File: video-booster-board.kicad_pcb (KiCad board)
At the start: 4 copper layers, 36.5 x 41.5 mm, 122 parts, among them J1 0473460001, J10 MC-HVT1-S04-G, J2 HDMI-PE10-19-LF, J3 HDMI-PE10-19-LF, J4 M20-9990246, J5 M20-9990246, J6 685119134923_, J7 M20-9990246, J8 M20-9990246, J9 685119134923_, Q1 BC817W, Q2 BC817W, U1 PTN3363, U2 EFM32HG309, U3 PTN3363, U4 LP2985-33DBVR, U5 PCA9554BS3, U6 PCA9517ADP, U7 PCA9517ADP

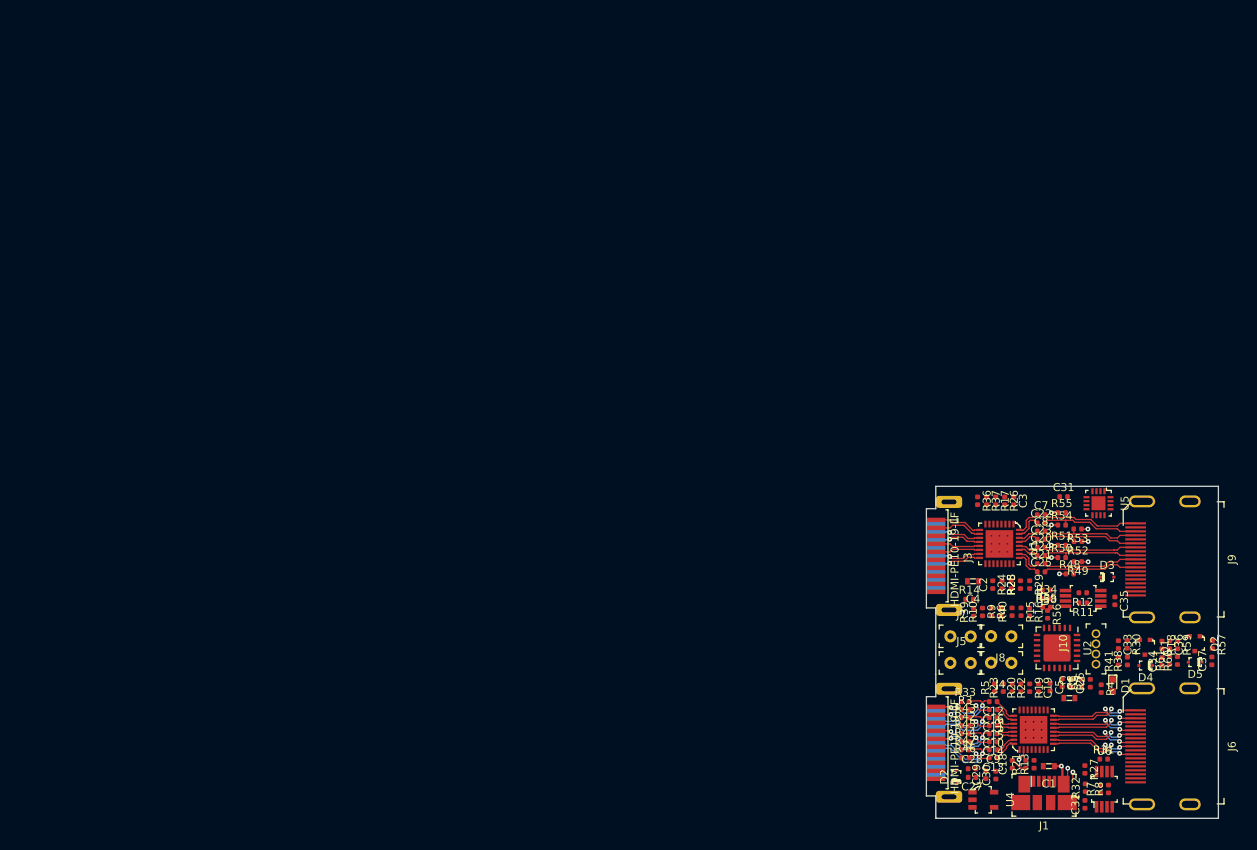
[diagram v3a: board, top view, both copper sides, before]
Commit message: Pinout adjustments. Placement of new components
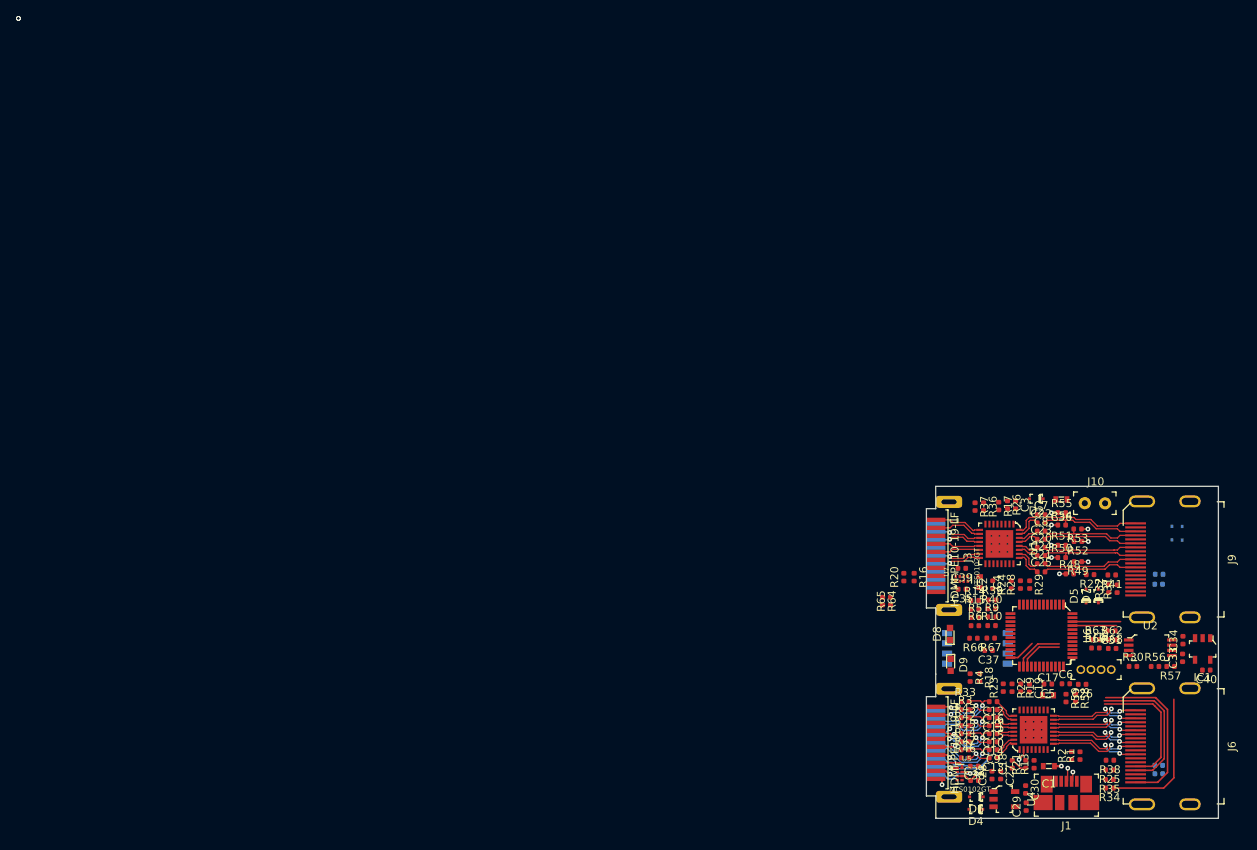
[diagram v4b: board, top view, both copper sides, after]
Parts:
- removed J4, J5, J7, J8: M20-9990246, antmicro-footprints:PinHeader_1x2_P2.54mm
- removed Q1, Q2: BC817W, antmicro-footprints:SOT-323
- removed R60: R_27k_0402, antmicro-footprints:0402-res
- removed R61: R_220R_0402, antmicro-footprints:0402-res
- added C38: C_100n_0402_6V3, antmicro-footprints:0402-cap, F.Cu at (119.5, 93.5)
- added C39: C_100n_0402_6V3, antmicro-footprints:0402-cap, F.Cu at (117.9, 68.8)
- added C40: C_100n_0402_6V3, antmicro-footprints:0402-cap, F.Cu at (148.5, 81.5)
- added D6: BAT54-02V-V-G, antmicro-footprints:SOD-523, F.Cu at (119.7, 97.3)
- added D7: BAT54-02V-V-G, antmicro-footprints:SOD-523, F.Cu at (135.0, 72.2)
- added D8: LG_L29K-G2J1-24-Z, antmicro-footprints:LED_0603, F.Cu at (116.5, 77.0)
- added D9: LG_L29K-G2J1-24-Z, antmicro-footprints:LED_0603, F.Cu at (116.5, 80.8)
- added IC1: INA180A1IDBVT, antmicro-footprints:SOT-23-5, F.Cu at (148.0, 78.8)
- added J11: MC-HVT1-S04-G, antmicro-footprints:PinHeader_1x4_P1.27mm_Drill.7mm, F.Cu at (132.8, 81.4)
- added R62: R_27k_0402, antmicro-footprints:0402-res, F.Cu at (136.7, 77.7)
- added R63: R_4k7_0402, antmicro-footprints:0402-res, F.Cu at (134.6, 77.7)
- added R64: R_27k_0402, antmicro-footprints:0402-res, F.Cu at (108.0, 72.8)
- added R65: R_4k7_0402, antmicro-footprints:0402-res, F.Cu at (109.0, 72.8)
- added R66: R_330R_0402, antmicro-footprints:0402-res, F.Cu at (119.4, 77.5)
- added R67: R_330R_0402, antmicro-footprints:0402-res, F.Cu at (121.5, 77.5)
- added R68: R_27k_0402, antmicro-footprints:0402-res, F.Cu at (136.7, 78.8)
- added R69: R_4k7_0402, antmicro-footprints:0402-res, F.Cu at (134.6, 78.7)
- added SW1: 1571983-5, antmicro-footprints:1571983-5, B.Cu at (119.9, 78.8)
- C33: value C_220p_0402 -> C_100n_0402_6V3
- C34, C37: value C_220p_0402 -> C_1u_0402
- C36: value C_220p_0402 -> C_4u7_0603; footprint antmicro-footprints:0402-cap -> antmicro-footprints:0603-cap
- D1: value LG_L29K-G2J1-24-Z -> BAT54-02V-V-G; footprint antmicro-footprints:LED_0603 -> antmicro-footprints:SOD-523; moved to B.Cu
- D3, R11, R12, R7, R8: moved to B.Cu
- D4, D5: value 1N4148X-TP -> BAT54-02V-V-G
- J10: value MC-HVT1-S04-G -> M20-9990246; footprint antmicro-footprints:PinHeader_1x4_P1.27mm_Drill.7mm -> antmicro-footprints:PinHeader_1x2_P2.54mm
- R16: value R_18k_0402 -> R_100R_0402
- R18, R20, R25, R27: value R_100k_0402 -> R_27k_0402
- R30: value R_47k_0402 -> R_806k_0402
- R38: value R_27k_0402 -> R_100R_0402
- R4: value R_330R_0402 -> R_100R_0402
- R41: value R_220R_0402 -> R_100R_0402
- R56: value R_18k_0402 -> R_1R_0402
- R57: value R_100k_0402 -> R_1R_0402
- R58: value R_100k_0402 -> R_10k_0402
- R59: value R_47k_0402 -> R_10k_0402
- U2: value EFM32HG309 -> TPS2110APW; footprint antmicro-footprints:QFN-24-1EP_5x5mm -> antmicro-footprints:TSSOP-8_W4.4mm
- U5: value PCA9554BS3 -> NTS0102GT; footprint antmicro-footprints:VFQFN-16-1EP_3x3mm -> antmicro-footprints:PSON50P100X195X50-8N
- U6: value PCA9517ADP -> EFM32HG321; footprint antmicro-footprints:TSSOP-8_W3mm -> antmicro-footprints:TQFP-48_7x7mm
- U7: value PCA9517ADP -> NTS0102GT; footprint antmicro-footprints:TSSOP-8_W3mm -> antmicro-footprints:PSON50P100X195X50-8N
- moved U5 38.0 mm to (117.7, 94.5), turned to 0 degrees
- moved D2 36.2 mm to (127.2, 60.0), turned to 180 degrees
- moved C37 27.9 mm to (121.3, 79.0), turned to 180 degrees
- moved D4 27.8 mm to (119.7, 98.9)
- moved R25 26.8 mm to (136.4, 93.9), turned to 180 degrees
- moved R32 25.1 mm to (136.3, 71.3)
- moved R34 24.9 mm to (136.4, 96.2), turned to 180 degrees
- moved R27 24.4 mm to (134.0, 69.5), turned to 180 degrees
- moved R18 23.1 mm to (120.2, 82.4)
- moved R35 22.9 mm to (136.4, 95.2), turned to 180 degrees
- moved C36 22.6 mm to (130.4, 60.1), turned to 180 degrees
- moved R31 21.4 mm to (137.3, 71.3), turned to 90 degrees
- moved U6 20.8 mm to (127.9, 77.2), turned to 270 degrees
- moved D1 20.4 mm to (144.2, 64.3)
- moved J10 20.2 mm to (133.3, 60.6), turned to 0 degrees
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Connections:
- C31 pad 1: GND -> +5VA
- C31 pad 2: VDD -> GND
- C32 pad 1: GND -> VDD
- C32 pad 2: /TX_5V -> GND
- C33 pad 1: /TX_CEC_IN -> GND
- C33 pad 2: GND -> /TX_SRC_5V
- C34 pad 1: /TX_CEC -> /TX_SINK_PWR
- C34 pad 2: Net-(C34-Pad2) -> GND
- C35 pad 1: GND -> VDD
- C35 pad 2: /RX_5V -> GND
- C36 pad 1: /RX_CEC_IN -> +5VA
- C37 pad 1: /RX_CEC -> VDD
- C37 pad 2: Net-(C37-Pad2) -> GND
- D2 pad A: /TX_5V -> GND
- D2 pad K: +5V -> +5VA
- D3 pad A: /RX_5V -> +5VA
- D3 pad K: +5V -> /RX_SINK_5V
- D4 pad A: Net-(D4-PadA) -> /VUSB
- D4 pad K: /TX_CEC -> +5V
- D5 pad A: Net-(D5-PadA) -> +5VA
- D5 pad K: /RX_CEC -> +5V
- J10 pad 1: GND -> +5VA
- J10 pad 2: /DBG_SWCLK -> GND
- J2 pad 13: /TX_CEC -> Net-(J2-Pad13)
- J2 pad 15: /SRC_TX_SCL -> /TX_SRC_SCL
- J2 pad 16: /SRC_TX_SDA -> /TX_SRC_SDA
- J2 pad 18: /TX_5V -> /TX_SRC_5V
- J3 pad 13: /RX_CEC -> Net-(J3-Pad13)
- J3 pad 15: /RX_SCL -> /RX_SINK_SCL
- J3 pad 16: /RX_SDA -> /RX_SINK_SDA
- J3 pad 18: /RX_5V -> /RX_SINK_5V
- J6 pad 13: /TX_CEC -> Net-(J6-Pad13)
- J6 pad 15: /TX_SCL -> /TX_SINK_SCL
- J6 pad 16: /TX_SDA -> /TX_SINK_SDA
- J6 pad 18: /TX_5V -> /TX_SINK_5V
- J9 pad 13: /RX_CEC -> Net-(J9-Pad13)
- J9 pad 15: /SRC_RX_SCL -> /RX_SRC_SCL
- J9 pad 16: /SRC_RX_SDA -> /RX_SRC_SDA
- J9 pad 18: /RX_5V -> /RX_SRC_5V
- R11 pad 1: /SRC_RX_SCL -> /RX_SINK_SDA
- R11 pad 2: /RX_SCL -> /RX_SRC_SDA
- R12 pad 1: /SRC_RX_SDA -> /RX_SINK_SCL
- R12 pad 2: /RX_SDA -> /RX_SRC_SCL
- R16 pad 1: VDD -> Net-(J3-Pad13)
- R16 pad 2: /TX_CEC_OUT -> /RX_SINK_CEC
- R18 pad 1: /TX_CEC_OUT -> /TX_SRC_CEC
- R18 pad 2: Net-(C34-Pad2) -> VDD
- R20 pad 1: /TX_DCC_EN -> /RX_SINK_CEC
- R20 pad 2: GND -> VDD
- R25 pad 1: /RX_DCC_EN -> /TX_SINK_CEC
- R25 pad 2: GND -> VDD
- R27 pad 1: /TX_I2C_PASS -> /RX_SRC_CEC
- R27 pad 2: /TX_5V -> VDD
- R30 pad 1: /TX_CEC_IN -> Net-(R30-Pad1)
- R30 pad 2: Net-(D4-PadA) -> GND
- R31 pad 1: +5V -> /RX_SRC_5V
- R31 pad 2: /TX_SDA -> /RX_SRC_SDA
- R32 pad 1: +5V -> /RX_SRC_5V
- R32 pad 2: /TX_SCL -> /RX_SRC_SCL
- R34 pad 1: +5V -> /TX_SINK_5V
- R34 pad 2: /RX_SDA -> /TX_SINK_SDA
- R35 pad 1: +5V -> /TX_SINK_5V
- R35 pad 2: /RX_SCL -> /TX_SINK_SCL
- R36 pad 2: /MCU_SDA -> /RX_SRC_SDA_3V
- R37 pad 2: /MCU_SCL -> /RX_SRC_SCL_3V
- R38 pad 1: VDD -> Net-(J6-Pad13)
- R38 pad 2: Net-(D4-PadA) -> /TX_SINK_CEC
- R4 pad 1: Net-(R4-Pad1) -> Net-(J2-Pad13)
- R4 pad 2: Net-(D1-Pad1) -> /TX_SRC_CEC
- R41 pad 1: Net-(Q1-Pad2) -> Net-(J9-Pad13)
- R41 pad 2: GND -> /RX_SRC_CEC
- R56 pad 1: VDD -> /TX_SINK_PWR
- R56 pad 2: /RX_CEC_OUT -> /TX_SINK_5V
- R57 pad 1: /RX_CEC_OUT -> /TX_SINK_PWR
- R57 pad 2: Net-(C37-Pad2) -> /TX_SINK_5V
- R58 pad 1: /RX_I2C_PASS -> VDD
- R58 pad 2: /RX_5V -> /TX_SINK_SDA_3V
- R59 pad 1: /RX_CEC_IN -> VDD
- R59 pad 2: Net-(D5-PadA) -> /TX_SINK_SCL_3V
- R7 pad 1: /SRC_TX_SCL -> /TX_SINK_SDA
- R7 pad 2: /TX_SCL -> /TX_SRC_SDA
- R8 pad 1: /SRC_TX_SDA -> /TX_SINK_SCL
- R8 pad 2: /TX_SDA -> /TX_SRC_SCL
- U1 pad 19: /SRC_RX_SCL -> /RX_SRC_SCL
- U1 pad 20: /SRC_RX_SDA -> /RX_SRC_SDA
- U1 pad 5: /MCU_RX_HPD -> /RX_HPD_3V
- U1 pad 6: /MCU_SDA -> /RX_SRC_SDA_3V
- U1 pad 7: /MCU_SCL -> /RX_SRC_SCL_3V
- U2 pad 1: /MCU_RX_HPD -> /PWR_CTL_D0
- U2 pad 2: VDD -> /PWR_CTL_D1
- U2 pad 3: /RX_CEC_OUT -> +5VA
- U2 pad 4: /TX_CEC_OUT -> Net-(R30-Pad1)
- U2 pad 5: /TX_CEC_IN -> GND
- U2 pad 6: /RX_CEC_IN -> /TX_SRC_5V
- U2 pad 7: Net-(U2-Pad7) -> /TX_SINK_PWR
- U2 pad 8: /RX_DCC_EN -> +5VA
- U3 pad 19: /SRC_TX_SCL -> /TX_SINK_SCL
- U3 pad 20: /SRC_TX_SDA -> /TX_SINK_SDA
- U3 pad 5: /MCU_TX_HPD -> /TX_HPD_3V
- U3 pad 6: /MCU_SDA -> /TX_SINK_SDA_3V
- U3 pad 7: /MCU_SCL -> /TX_SINK_SCL_3V
- U5 pad 1: GND -> /TX_SRC_SDA
- U5 pad 2: /TX_EQ0_R -> GND
- U5 pad 3: /TX_EQ1_R -> VDD
- U5 pad 4: /TX_DDET -> /TX_SRC_SDA_3V
- U5 pad 5: /TX_I2C_PASS -> /TX_SRC_SCL_3V
- U5 pad 6: GND -> VDD
- U5 pad 7: /RX_EQ0_R -> /TX_SRC_5V
- U5 pad 8: /RX_EQ1_R -> /TX_SRC_SCL
- U6 pad 1: /TX_5V -> /TX_SRC_SDA_3V
- U6 pad 2: /SRC_TX_SCL -> /TX_SRC_SCL_3V
- U6 pad 3: /SRC_TX_SDA -> /TX_DDET
- U6 pad 4: GND -> VDD
- U6 pad 5: /TX_I2C_PASS -> GND
- U6 pad 6: /TX_SDA -> /RX_SRC_SDA_3V
- U6 pad 7: /TX_SCL -> /RX_SRC_SCL_3V
- U6 pad 8: /TX_5V -> /RX_SINK_SDA_3V
- U7 pad 1: /RX_5V -> /RX_SINK_SDA
- U7 pad 2: /SRC_RX_SCL -> GND
- U7 pad 3: /SRC_RX_SDA -> VDD
- U7 pad 4: GND -> /RX_SINK_SDA_3V
- U7 pad 5: /RX_I2C_PASS -> /RX_SINK_SCL_3V
- U7 pad 6: /RX_SDA -> VDD
- U7 pad 7: /RX_SCL -> /RX_SINK_5V
- U7 pad 8: /RX_5V -> /RX_SINK_SCL
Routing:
- net /TX_HPD: track 0.00 -> 22.1 mm, vias 0 -> 1
- net /TX_SINK_SDA: track 0.00 -> 18.2 mm
- net /TX_SINK_5V: track 0.00 -> 17.9 mm
- net /TX_SINK_SCL: track 0.00 -> 16.8 mm
- net Net-(J2-Pad13): track 0.00 -> 9.70 mm, vias 0 -> 1
- net /TX_UTILITY: track 0.00 -> 7.42 mm
- net GND: track 0.00 -> 7.40 mm, vias 0 -> 3
- net /ADC6: track 0.00 -> 6.27 mm
- net /PWR_CTL_D1: track 0.00 -> 6.03 mm
- net /TX_SRC_5V: track 0.00 -> 5.85 mm, vias 0 -> 1
- net /ADC7: track 0.00 -> 5.55 mm
- net /PWR_CTL_D0: track 0.00 -> 5.52 mm
- net /TX_SRC_SCL: track 0.00 -> 3.75 mm
- net /ADC4: track 0.00 -> 3.44 mm
- net VDD: track 8.56 -> 11.6 mm, vias 8 -> 9
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
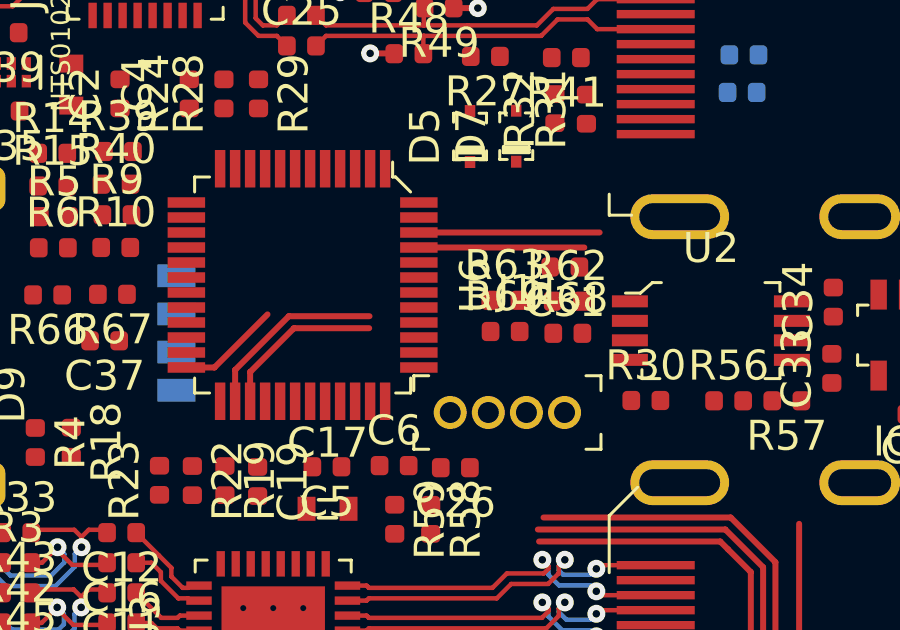
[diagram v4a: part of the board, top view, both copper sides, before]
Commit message: CEC clamp diodes added. Open hardware logo added
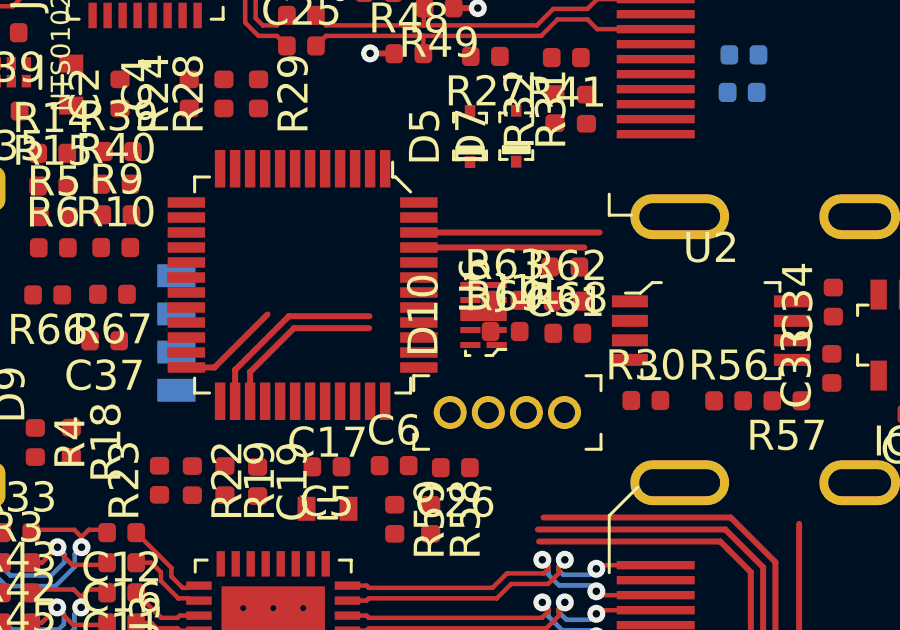
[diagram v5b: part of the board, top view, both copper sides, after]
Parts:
- added D10: RCLAMP0524PATCT, antmicro-footprints:UFDFN-10_2.5x1mm, F.Cu at (133.9, 78.2)
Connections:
- net VDD renamed +3V3

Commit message: Local libraries generated. SCH and PCB relinked to local libraries
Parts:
- C1, C17, C36, C4: footprint antmicro-footprints:0603-cap -> video-booster-board-footprints:0603-cap
- C10, C11, C12, C13, C14, C15, C16, C18, C19, C2, C20, C21, C22, C23, C24, C25, C26, C27, C28, C29, C3, C30, C31, C32, C33, C34, C35, C37, C38, C39, C40, C5, C6, C7, C8, C9: footprint antmicro-footprints:0402-cap -> video-booster-board-footprints:0402-cap
- D1, D2, D3, D4, D5, D6, D7: footprint antmicro-footprints:SOD-523 -> video-booster-board-footprints:SOD-523
- D10: footprint antmicro-footprints:UFDFN-10_2.5x1mm -> video-booster-board-footprints:UFDFN-10_2.5x1mm
- D8, D9: footprint antmicro-footprints:LED_0603 -> video-booster-board-footprints:LED_0603
- IC1: footprint antmicro-footprints:SOT-23-5 -> video-booster-board-footprints:SOT-23-5
- J1: footprint antmicro-footprints:USB_Micro_B_Female_0473460001 -> video-booster-board-footprints:USB_Micro_B_Female_0473460001
- J10: footprint antmicro-footprints:PinHeader_1x2_P2.54mm -> video-booster-board-footprints:PinHeader_1x2_P2.54mm
- J11: footprint antmicro-footprints:PinHeader_1x4_P1.27mm_Drill.7mm -> video-booster-board-footprints:PinHeader_1x4_P1.27mm_Drill.7mm
- J2, J3: footprint antmicro-footprints:HDMI-PE10-19-LF -> video-booster-board-footprints:HDMI-PE10-19-LF
- J6, J9: footprint antmicro-footprints:HDMI_A_Female_685119134923 -> video-booster-board-footprints:HDMI_A_Female_685119134923
- R1, R10, R11, R12, R13, R14, R15, R16, R17, R18, R19, R2, R20, R21, R22, R23, R24, R25, R26, R27, R28, R29, R3, R30, R31, R32, R33, R34, R35, R36, R37, R38, R39, R4, R40, R41, R42, R43, R44, R45, R46, R47, R48, R49, R5, R50, R51, R52, R53, R54, R55, R56, R57, R58, R59, R6, R62, R63, R64, R65, R66, R67, R68, R69, R7, R8, R9: footprint antmicro-footprints:0402-res -> video-booster-board-footprints:0402-res
- SW1: footprint antmicro-footprints:1571983-5 -> video-booster-board-footprints:1571983-5
- U1, U3: footprint antmicro-footprints:QFN-32-1EP_5x5mm -> video-booster-board-footprints:QFN-32-1EP_5x5mm
- U2: footprint antmicro-footprints:TSSOP-8_W4.4mm -> video-booster-board-footprints:TSSOP-8_W4.4mm
- U4: footprint antmicro-footprints:SOT-753 -> video-booster-board-footprints:SOT-753
- U5, U7: footprint antmicro-footprints:PSON50P100X195X50-8N -> video-booster-board-footprints:PSON50P100X195X50-8N
- U6: footprint antmicro-footprints:TQFP-48_7x7mm -> video-booster-board-footprints:TQFP-48_7x7mm
